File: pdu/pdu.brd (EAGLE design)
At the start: 17.5 x 90 mm, 54 parts, among them IC1 FDN359BN, IC2 FDN359BN, IC3 FDN359BN, J1 S2B-PH-K-S(LF)(SN), J10 S2B-PH-K-S(LF)(SN), J2 S2B-PH-K-S(LF)(SN), J3 S2B-PH-K-S(LF)(SN), J4 S2B-PH-K-S(LF)(SN), J5 S2B-PH-K-S(LF)(SN), J6 S2B-PH-K-S(LF)(SN), J7 S2B-PH-K-S(LF)(SN), J8 S2B-PH-K-S(LF)(SN), J9 S2B-PH-K-S(LF)(SN)

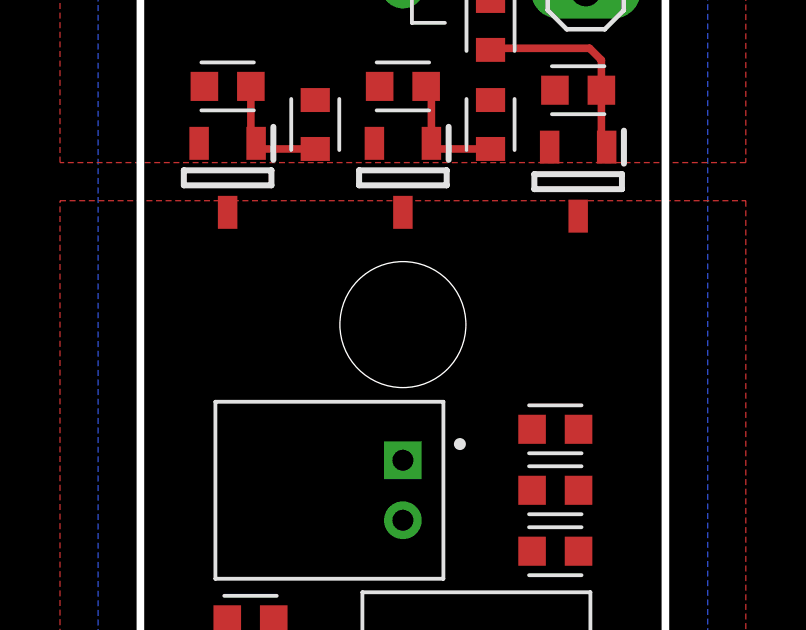
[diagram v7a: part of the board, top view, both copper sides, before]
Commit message: add status leds
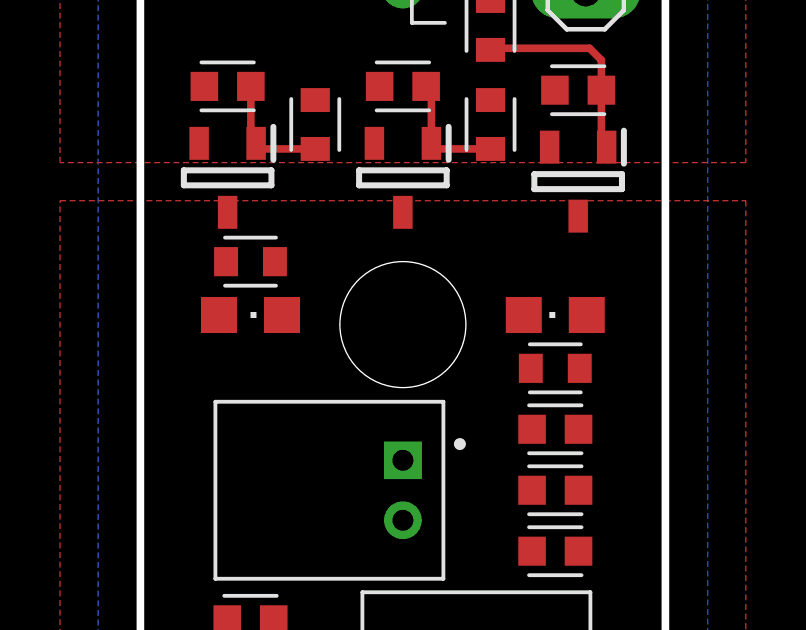
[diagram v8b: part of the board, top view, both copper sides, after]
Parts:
- added LED2: LEDY, adafruit:CHIPLED_0805
- added LED3: LEDG, adafruit:CHIPLED_0805
- added R4: 120, Resistor:RESC1608X60
- added R6: 100, Resistor:RESC1608X60
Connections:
- new net N$4: LED3.C, R6.2
- new net N$5: LED2.C, R4.1
- net GND: now also R6.1
- net RET: now also R4.2
- net VBAT: now also LED2.A, LED3.A
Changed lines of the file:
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@@
 <attribute name="VALUE" x="7.2" y="-33.272" size="0.6096" layer="27" rot="R90"/>
+</element>
+<element name="LED2" library="adafruit" library_urn="urn:adsk.eagle:library:420" package="CHIPLED_0805" package3d_urn="urn:adsk.eagle:package:6240559/1" value="LEDY" x="5.08" y="20.32" smashed="yes" rot="R90">
+<attribute name="VALUE" x="6.35" y="22.86" size="1.27" layer="27" rot="R180"/>
+</element>
+<element name="R4" library="Resistor" library_urn="urn:adsk.eagle:library:16378527" package="RESC1608X60" package3d_urn="urn:adsk.eagle:package:16378565/5" value="120" x="5.08" y="18.542" smashed="yes">
+<attribute name="CATEGORY" value="Resistor" x="0" y="18.542" size="1.778" layer="27" font="vector" ratio="15" display="off"/>
+<attribute name="MANUFACTURER" value="" x="0" y="18.542" size="1.778" layer="27" font="vector" ratio="15" display="off"/>
+<attribute name="MPN" value="" x="0" y="18.542" size="1.778" layer="27" font="vector" ratio="15" display="off"/>
+<attribute name="OPERATING_TEMP" value="" x="0" y="18.542" size="1.778" layer="27" font="vector" ratio="15" display="off"/>
+<attribute name="PART_STATUS" value="" x="0" y="18.542" size="1.778" layer="27" font="vector" ratio="15" display="off"/>
+<attribute name="RATING" value="" x="0" y="18.542" size="1.778" layer="27" font="vector" ratio="15" display="off"/>
+<attribute name="ROHS_COMPLIANT" value="" x="0" y="18.542" size="1.778" layer="27" font="vector" ratio="15" display="off"/>
+<attribute name="SERIES" value="" x="0" y="18.542" size="1.778" layer="27" font="vector" ratio="15" display="off"/>
+<attribute name="SUB-CATEGORY" value="Fixed" x="0" y="18.542" size="1.778" layer="27" font="vector" ratio="15" display="off"/>
+<attribute name="THERMALLOSS" value="" x="0" y="18.542" size="1.778" layer="27" font="vector" ratio="15" display="off"/>
+<attribute name="TOLERANCE" value="" x="0" y="18.542" size="1.778" layer="27" font="vector" ratio="15" display="off"/>
+<attribute name="TYPE" value="" x="0" y="18.542" size="1.778" layer="27" font="vector" ratio="15" display="off"/>
+<attribute name="VALUE" x="5.08" y="17.1061" size="1.27" layer="27" align="top-center"/>
+</element>
+<element name="R6" library="Resistor" library_urn="urn:adsk.eagle:library:16378527" package="RESC1608X60" package3d_urn="urn:adsk.eagle:package:16378565/5" value="100" x="-5.08" y="22.098" smashed="yes">
+<attribute name="CATEGORY" value="Resistor" x="-15.24" y="14.478" size="1.778" layer="27" font="vector" ratio="15" display="off"/>
+<attribute name="MANUFACTURER" value="" x="-15.24" y="14.478" size="1.778" layer="27" font="vector" ratio="15" display="off"/>
+<attribute name="MPN" value="" x="-15.24" y="14.478" size="1.778" layer="27" font="vector" ratio="15" display="off"/>
+<attribute name="OPERATING_TEMP" value="" x="-15.24" y="14.478" size="1.778" layer="27" font="vector" ratio="15" display="off"/>
+<attribute name="PART_STATUS" value="" x="-15.24" y="14.478" size="1.778" layer="27" font="vector" ratio="15" display="off"/>
+<attribute name="RATING" value="" x="-15.24" y="14.478" size="1.778" layer="27" font="vector" ratio="15" display="off"/>
+<attribute name="ROHS_COMPLIANT" value="" x="-15.24" y="14.478" size="1.778" layer="27" font="vector" ratio="15" display="off"/>
+<attribute name="SERIES" value="" x="-15.24" y="14.478" size="1.778" layer="27" font="vector" ratio="15" display="off"/>
+<attribute name="SUB-CATEGORY" value="Fixed" x="-15.24" y="14.478" size="1.778" layer="27" font="vector" ratio="15" display="off"/>
+<attribute name="THERMALLOSS" value="" x="-15.24" y="14.478" size="1.778" layer="27" font="vector" ratio="15" display="off"/>
+<attribute name="TOLERANCE" value="" x="-15.24" y="14.478" size="1.778" layer="27" font="vector" ratio="15" display="off"/>
+<attribute name="TYPE" value="" x="-15.24" y="14.478" size="1.778" layer="27" font="vector" ratio="15" display="off"/>
+<attribute name="VALUE" x="-5.08" y="20.6621" size="1.27" layer="27" align="top-center"/>
+</element>
+<element name="LED3" library="adafruit" library_urn="urn:adsk.eagle:library:420" package="CHIPLED_0805" package3d_urn="urn:adsk.eagle:package:6240559/1" value="LEDG" x="-5.08" y="20.32" smashed="yes" rot="R270">
+<attribute name="VALUE" x="-6.35" y="17.78" size="1.27" layer="27"/>
 </element>
 </elements>
@@
 <vertex x="-11.43" y="25.4"/>
 </polygon>
+<contactref element="R6" pad="1"/>
+<wire x1="-6.792" y1="26.042" x2="-5.8952" y2="22.098" width="0" layer="19" extent="1-1"/>
+<wire x1="-6.6166" y1="27.94" x2="-6.792" y2="26.042" width="0" layer="19" extent="1-1"/>
+<wire x1="-0.7746" y1="27.94" x2="-6.6166" y2="27.94" width="0" layer="19" extent="1-1"/>
+<wire x1="-0.95" y1="26.042" x2="-0.7746" y2="27.94" width="0" layer="19" extent="1-1"/>
+<wire x1="0" y1="33.258" x2="-0.7746" y2="27.94" width="0" layer="19" extent="1-1"/>
+<wire x1="-0.8152" y1="36.576" x2="0" y2="33.258" width="0" layer="19" extent="1-1"/>
+<wire x1="-4.588" y1="37.465" x2="-0.8152" y2="36.576" width="0" layer="19" extent="1-1"/>
+<wire x1="4.892" y1="25.915" x2="-0.95" y2="26.042" width="0" layer="19" extent="1-1"/>
+<wire x1="5.0674" y1="27.813" x2="4.892" y2="25.915" width="0" layer="19" extent="1-1"/>
+<wire x1="6.588" y1="37.211" x2="-0.8152" y2="36.576" width="0" layer="19" extent="1-1"/>
 </signal>
 <signal name="VBAT">
@@
 <contactref element="C32" pad="2"/>
 <contactref element="J9" pad="2"/>
-<wire x1="-5.588" y1="-33.6424" x2="-7.747" y2="-33.6424" width="0" layer="19" extent="1-1"/>
+<contactref element="LED3" pad="A"/>
+<contactref element="LED2" pad="A"/>
+<wire x1="-6.13" y1="20.32" x2="6.13" y2="20.32" width="0" layer="19" extent="1-1"/>
+<wire x1="-4.588" y1="-37.211" x2="-6.13" y2="20.32" width="0" layer="19" extent="1-1"/>
+<wire x1="-5.588" y1="-33.6424" x2="-4.588" y2="-37.211" width="0" layer="19" extent="1-1"/>
 <wire x1="-5.8546" y1="-32.004" x2="-5.588" y2="-33.6424" width="0" layer="19" extent="1-1"/>
 <wire x1="-5.8546" y1="-29.972" x2="-5.8546" y2="-32.004" width="0" layer="19" extent="1-1"/>
 <wire x1="-5.8546" y1="-27.94" x2="-5.8546" y2="-29.972" width="0" layer="19" extent="1-1"/>
+<wire x1="-7.747" y1="-33.6424" x2="-5.588" y2="-33.6424" width="0" layer="19" extent="1-1"/>
 <wire x1="-3.429" y1="-33.6424" x2="-5.588" y2="-33.6424" width="0" layer="19" extent="1-1"/>
-<wire x1="-4.588" y1="-37.211" x2="-5.588" y2="-33.6424" width="0" layer="19" extent="1-1"/>
 <wire x1="0" y1="-28.972" x2="-3.429" y2="-33.6424" width="0" layer="19" extent="1-1"/>
 <wire x1="0" y1="-24.622" x2="0" y2="-28.972" width="0" layer="19" extent="1-1"/>
@@
 <contactref element="C33" pad="1"/>
 <contactref element="J9" pad="1"/>
-<wire x1="-5.588" y1="-35.1916" x2="-7.747" y2="-35.1916" width="0" layer="19" extent="1-1"/>
+<contactref element="R4" pad="2"/>
+<wire x1="-6.588" y1="-37.211" x2="5.8952" y2="18.542" width="0" layer="19" extent="1-1"/>
+<wire x1="-5.588" y1="-35.1916" x2="-6.588" y2="-37.211" width="0" layer="19" extent="1-1"/>
+<wire x1="-7.747" y1="-35.1916" x2="-5.588" y2="-35.1916" width="0" layer="19" extent="1-1"/>
 <wire x1="-3.429" y1="-35.1916" x2="-5.588" y2="-35.1916" width="0" layer="19" extent="1-1"/>
-<wire x1="-6.588" y1="-37.211" x2="-5.588" y2="-35.1916" width="0" layer="19" extent="1-1"/>
 <wire x1="-4.3054" y1="-32.004" x2="-3.429" y2="-35.1916" width="0" layer="19" extent="1-1"/>
 <wire x1="-4.3054" y1="-29.972" x2="-4.3054" y2="-32.004" width="0" layer="19" extent="1-1"/>
@@
 <wire x1="-5.842" y1="23.742" x2="0" y2="23.742" width="0" layer="19" extent="1-1"/>
 </signal>
+<signal name="N$4">
+<contactref element="LED3" pad="C"/>
+<contactref element="R6" pad="2"/>
+<wire x1="-4.2648" y1="22.098" x2="-4.03" y2="20.32" width="0" layer="19" extent="1-1"/>
+</signal>
+<signal name="N$5">
+<contactref element="LED2" pad="C"/>
+<contactref element="R4" pad="1"/>
+<wire x1="4.2648" y1="18.542" x2="4.03" y2="20.32" width="0" layer="19" extent="1-1"/>
+</signal>
 </signals>
